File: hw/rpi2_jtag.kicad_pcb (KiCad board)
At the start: 2 copper layers, 33 x 35.6 mm, 11 parts, among them J20 CONN_02X10, P1 CONN_01X13, P2 CONN_01X13

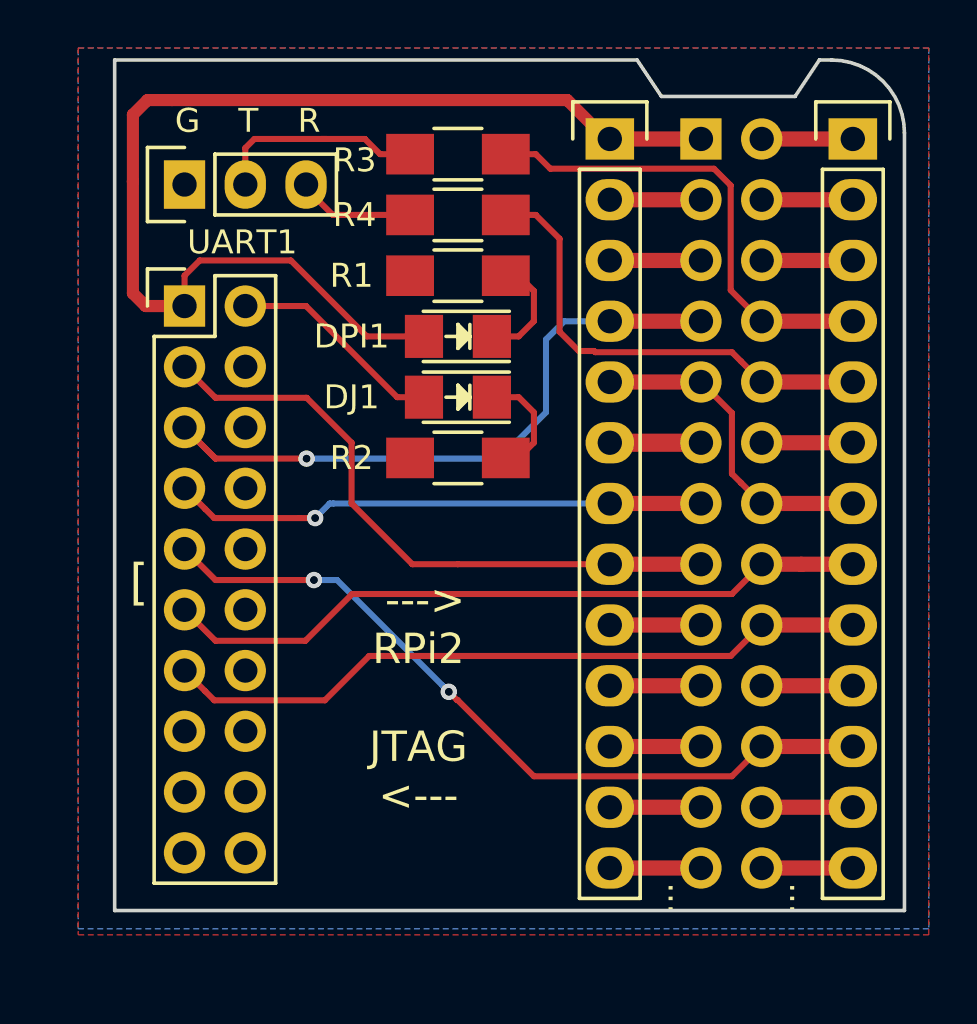
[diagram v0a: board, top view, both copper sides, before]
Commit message: v0.3: corrected RX/TX pins, added voltage divider to RX. changed JTAG connector to IDC-20 v0.x: added License and fixed missing grebers. updated README with links
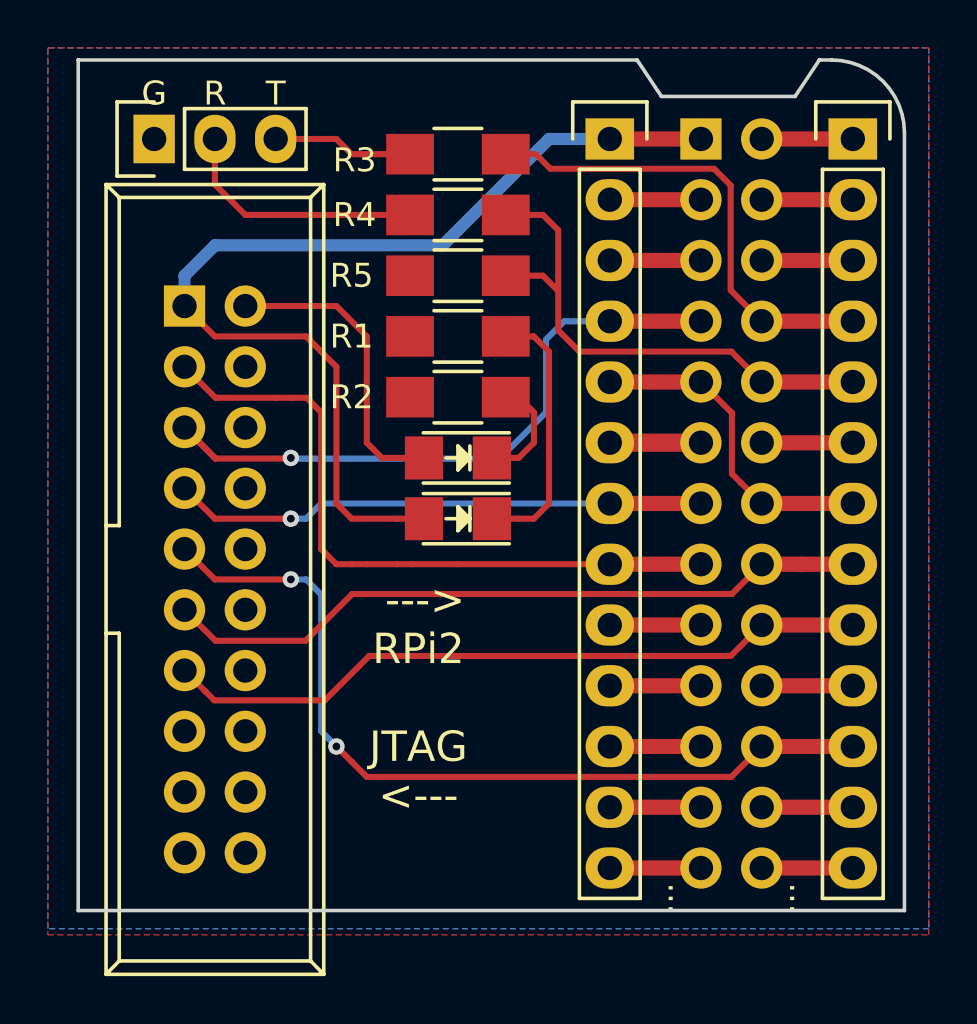
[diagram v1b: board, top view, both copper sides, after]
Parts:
- added R5: 1K, Resistors_SMD:R_1206_HandSoldering, F.Cu at (87.0, 98.4)
- J20: footprint Pin_Headers:Pin_Header_Straight_2x10 -> Connect:IDC_Header_Straight_20pins
- R3: value 470 -> 100
- R4: value 100 -> 470
- moved DPI1 7.62 mm to (87.0, 108.6)
- moved DJ1 2.54 mm to (87.0, 106.0)
- moved R1 2.54 mm to (87.0, 101.0)
- moved R2 2.54 mm to (87.0, 103.5)
- moved UART1 2.29 mm to (74.3, 92.7)
- turned J20 to 270 degrees
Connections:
- P1 pad 13: Net-(P1-Pad13) -> GND
- P2 pad 10: Net-(P2-Pad10) -> GND
- PI2 pad 20: Net-(P2-Pad10) -> GND
- PI2 pad 25: Net-(P1-Pad13) -> GND
- UART1 pad 2: Net-(R3-Pad1) -> Net-(R4-Pad1)
- UART1 pad 3: Net-(R4-Pad1) -> Net-(R3-Pad1)
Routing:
- net GND: track 18.2 -> 25.8 mm
- net Net-(DPI1-Pad1): track 4.73 -> 11.1 mm
- net Net-(R4-Pad1): track 4.97 -> 10.6 mm
- net 3v3: track 47.4 -> 42.3 mm
- net Net-(P2-Pad10): track 3.81 -> 0.00 mm
- net Net-(P1-Pad13): track 3.81 -> 0.00 mm
- net JTAG_3v3: track 9.05 -> 12.7 mm
- net TCK: track 33.7 -> 37.0 mm
- net Net-(R3-Pad1): track 9.09 -> 5.88 mm
- net RX0: track 20.7 -> 23.3 mm
- net TDI: track 28.1 -> 30.0 mm
- net nTRST: track 26.5 -> 28.4 mm
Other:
- board size 33 x 35.6 mm -> 34.5 x 35.6 mm
- board text added: "RPi2-jtag v0.3"
- board text removed: "RPi2-jtag v0.2"
- board text removed: "["
